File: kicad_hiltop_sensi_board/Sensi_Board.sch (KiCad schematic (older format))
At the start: 146 parts, among them J1 Conn_02x06_Counter_Clockwise, J10 Conn_ARM_JTAG_SWD_10, J2 Conn_02x06_Counter_Clockwise, J3 Conn_03x32_DIN41612, J4 Conn_02x06_Counter_Clockwise, J5 Conn_02x06_Counter_Clockwise, J6 Conn_02x06_Counter_Clockwise, J7 Conn_02x06_Counter_Clockwise, J8 Conn_02x06_Counter_Clockwise, U1 INA250A4, U2 LD1117S33TR_SOT223, U3 AT25DN512CSSHF-B, U6 LM75B

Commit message: Most major connections complete and differential tracking done on the Sensi board layout
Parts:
- added J9: Conn_02x06_Counter_Clockwise, Devtank_PCB_Lib:Molex2x06, symbol Connector:Conn_02x06_Counter_Clockwise
- added TP106, TP107, TP99: Test_Point, TestPoint:TestPoint_THTPad_D1.0mm_Drill0.5mm, symbol Sensi_Board-rescue:Test_Point-Connector
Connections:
- net labels removed: +12V_EXT
- wire segments 530 -> 537
- no-connect marks 74 -> 77
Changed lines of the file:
@@
 $EndComp
 $Comp
-L Devtank:+12V_EXT #PWR041
-U 1 1 5C4F3E8E
-P 21125 11025
-F 0 "#PWR041" H 21125 10875 50  0001 C CNN
-F 1 "+12V_EXT" H 21140 11198 50  0000 C CNN
-F 2 "" H 21125 11025 50  0001 C CNN
-F 3 "" H 21125 11025 50  0001 C CNN
-	1    21125 11025
-	1    0    0    -1
-$EndComp
-$Comp
 L Sensi_Board-rescue:Conn_03x32_DIN41612-Devtank J3
 U 1 1 5C5BC2B2
@@
 	20300 11200 21125 11200
 Wire Wire Line
-	21125 11200 21125 11100
-Wire Wire Line
 	18425 11050 17750 11050
 Wire Wire Line
@@
 	0    1    1    0
 $EndComp
-Connection ~ 21125 11200
 $Comp
 L Sensi_Board-rescue:Test_Point-Connector TP87
@@
 Wire Wire Line
 	6450 8600 6050 8600
-$Comp
-L power:PWR_FLAG #FLG0103
-U 1 1 5F48A9D2
-P 21375 11000
-F 0 "#FLG0103" H 21375 11075 50  0001 C CNN
-F 1 "PWR_FLAG" H 21375 11173 50  0000 C CNN
-F 2 "" H 21375 11000 50  0001 C CNN
-F 3 "" H 21375 11000 50  0001 C CNN
-	1    21375 11000
-	1    0    0    -1
-$EndComp
-Wire Wire Line
-	21375 11000 21375 11100
-Wire Wire Line
-	21375 11100 21125 11100
-Connection ~ 21125 11100
-Wire Wire Line
-	21125 11100 21125 11025
 Text Label 16300 9700 2    60   ~ 0
 STM_SPI1_MISO
@@
 Wire Wire Line
 	10300 7300 10650 7300
-Text Label 10650 7300 2    60   ~ 0
+Text Label 10650 7500 2    60   ~ 0
 F3+
-Text Label 10650 7200 2    60   ~ 0
+Text Label 10650 7600 2    60   ~ 0
 F3-
 Wire Wire Line
@@
 	1    0    0    -1
 $EndComp
-$Comp
-L Connector:Conn_02x06_Counter_Clockwise J5
-U 1 1 5E20E350
-P 7150 14425
-F 0 "J5" H 7200 14842 50  0000 C CNN
-F 1 "Conn_02x06_Counter_Clockwise" H 7200 14751 50  0000 C CNN
-F 2 "Devtank_PCB_Lib:Molex2x06" H 7150 14425 50  0001 C CNN
-F 3 "~" H 7150 14425 50  0001 C CNN
-F 4 "711-004" H 7150 14425 50  0001 C CNN "Devtank"
-	1    7150 14425
-	1    0    0    -1
-$EndComp
 Wire Wire Line
-	6950 14225 6525 14225
-Text Label 6525 14225 0    60   ~ 0
+	6950 14725 6525 14725
+Text Label 7875 14225 2    60   ~ 0
 ADC7
 Wire Wire Line
-	6950 14425 6525 14425
-Text Label 6525 14425 0    60   ~ 0
+	7450 14425 7875 14425
+Text Label 7875 14425 2    60   ~ 0
 ADC13
 Wire Wire Line
-	6950 14625 6525 14625
-Text Label 6525 14625 0    60   ~ 0
+	7450 14625 7875 14625
+Text Label 7875 14625 2    60   ~ 0
 ADC12
 Wire Wire Line
 	7450 14225 7875 14225
-Text Label 7875 14225 2    60   ~ 0
+Text Label 6525 14725 0    60   ~ 0
 ADC6
-NoConn ~ 7450 14525
-NoConn ~ 7450 14425
 $Comp
 L Connector:Conn_02x06_Counter_Clockwise J6
@@
 	1    0    0    -1
 $EndComp
-Text Label 10650 7500 2    60   ~ 0
+Text Label 10650 7300 2    60   ~ 0
 F2-
-Text Label 10650 7600 2    60   ~ 0
+Text Label 10650 7200 2    60   ~ 0
 F2+
 Wire Wire Line
@@
 Wire Wire Line
 	9725 7600 9725 7675
-$Comp
-L power:GND #PWR0253
-U 1 1 5E212022
-P 6825 14800
-F 0 "#PWR0253" H 6825 14550 50  0001 C CNN
-F 1 "GND" H 6830 14627 50  0000 C CNN
-F 2 "" H 6825 14800 50  0001 C CNN
-F 3 "" H 6825 14800 50  0001 C CNN
-	1    6825 14800
-	-1   0    0    -1
-$EndComp
 Wire Wire Line
 	4500 11100 4325 11100
-Wire Wire Line
-	6950 14325 6825 14325
-Wire Wire Line
-	6825 14325 6825 14525
-Wire Wire Line
-	6950 14725 6825 14725
-Connection ~ 6825 14725
-Wire Wire Line
-	6825 14725 6825 14800
-Wire Wire Line
-	6950 14525 6825 14525
-Connection ~ 6825 14525
-Wire Wire Line
-	6825 14525 6825 14725
 $Comp
 L power:+3V3 #PWR0103
@@
 L power:GND #PWR0254
 U 1 1 5DABC198
-P 7625 14325
-F 0 "#PWR0254" H 7625 14075 50  0001 C CNN
-F 1 "GND" H 7630 14152 50  0000 C CNN
-F 2 "" H 7625 14325 50  0001 C CNN
-F 3 "" H 7625 14325 50  0001 C CNN
-	1    7625 14325
+P 7625 14775
+F 0 "#PWR0254" H 7625 14525 50  0001 C CNN
+F 1 "GND" H 7630 14602 50  0000 C CNN
+F 2 "" H 7625 14775 50  0001 C CNN
+F 3 "" H 7625 14775 50  0001 C CNN
+	1    7625 14775
 	1    0    0    -1
 $EndComp
 Wire Wire Line
 	7450 14325 7625 14325
-NoConn ~ 7450 14625
-NoConn ~ 7450 14725
 Text Label 8350 8550 2    60   ~ 0
 ADC11
@@
 Text Label 10750 10250 0    60   ~ 0
 RTD2_R-
+$Comp
+L Sensi_Board-rescue:Test_Point-Connector TP99
+U 1 1 5DB957A7
+P 16300 9700
+F 0 "TP99" V 16300 9875 50  0000 L CNN
+F 1 "Test_Point" H 16358 9729 50  0001 L CNN
+F 2 "TestPoint:TestPoint_THTPad_D1.0mm_Drill0.5mm" H 16500 9700 50  0001 C CNN
+F 3 "~" H 16500 9700 50  0001 C CNN
+	1    16300 9700
+	0    1    -1   0
+$EndComp
+$Comp
+L Sensi_Board-rescue:Test_Point-Connector TP106
+U 1 1 5DC01188
+P 16300 10000
+F 0 "TP106" V 16300 10175 50  0000 L CNN
+F 1 "Test_Point" H 16358 10029 50  0001 L CNN
+F 2 "TestPoint:TestPoint_THTPad_D1.0mm_Drill0.5mm" H 16500 10000 50  0001 C CNN
+F 3 "~" H 16500 10000 50  0001 C CNN
+	1    16300 10000
+	0    1    -1   0
+$EndComp
+$Comp
+L Sensi_Board-rescue:Test_Point-Connector TP107
+U 1 1 5DC6CAD7
+P 16300 10300
+F 0 "TP107" V 16300 10475 50  0000 L CNN
+F 1 "Test_Point" H 16358 10329 50  0001 L CNN
+F 2 "TestPoint:TestPoint_THTPad_D1.0mm_Drill0.5mm" H 16500 10300 50  0001 C CNN
+F 3 "~" H 16500 10300 50  0001 C CNN
+	1    16300 10300
+	0    1    -1   0
+$EndComp
+$Comp
+L Connector:Conn_02x06_Counter_Clockwise J9
+U 1 1 5DCD8F82
+P 18075 12225
+F 0 "J9" H 18125 12642 50  0000 C CNN
+F 1 "Conn_02x06_Counter_Clockwise" H 18125 12551 50  0000 C CNN
+F 2 "Devtank_PCB_Lib:Molex2x06" H 18075 12225 50  0001 C CNN
+F 3 "~" H 18075 12225 50  0001 C CNN
+F 4 "711-004" H 18075 12225 50  0001 C CNN "Devtank"
+	1    18075 12225
+	1    0    0    -1
+$EndComp
+$Comp
+L Devtank:ADJ_DC #PWR041
+U 1 1 5DCE41C9
+P 17550 12225
+F 0 "#PWR041" H 17550 12075 50  0001 C CNN
+F 1 "ADJ_DC" H 17425 12375 50  0000 L CNN
+F 2 "" H 17550 12225 50  0000 C CNN
+F 3 "" H 17550 12225 50  0000 C CNN
+	1    17550 12225
+	0    -1   -1   0
+$EndComp
+$Comp
+L Devtank:-5V #PWR057
+U 1 1 5DD68247
+P 18700 12125
+F 0 "#PWR057" H 18700 11975 50  0001 C CNN
+F 1 "-5V" V 18715 12253 50  0000 L CNN
+F 2 "" H 18700 12125 50  0000 C CNN
+F 3 "" H 18700 12125 50  0000 C CNN
+	1    18700 12125
+	0    1    -1   0
+$EndComp
+$Comp
+L power:+5V #PWR059
+U 1 1 5DD6824D
+P 18700 12025
+F 0 "#PWR059" H 18700 11875 50  0001 C CNN
+F 1 "+5V" V 18715 12153 50  0000 L CNN
+F 2 "" H 18700 12025 50  0001 C CNN
+F 3 "" H 18700 12025 50  0001 C CNN
+	1    18700 12025
+	0    1    -1   0
+$EndComp
+Text Label 17550 12025 0    60   ~ 0
+OUT1_NO
+Text Label 17550 12125 0    60   ~ 0
+OUT1_NC
+$Comp
+L power:+3V3 #PWR053
+U 1 1 5DCE41CF
+P 17550 12425
+F 0 "#PWR053" H 17550 12275 50  0001 C CNN
+F 1 "+3V3" H 17565 12598 50  0000 C CNN
+F 2 "" H 17550 12425 50  0001 C CNN
+F 3 "" H 17550 12425 50  0001 C CNN
+	1    17550 12425
+	0    -1   -1   0
+$EndComp
+$Comp
+L power:+12V #PWR052
+U 1 1 5E067E40
+P 17550 12325
+F 0 "#PWR052" H 17550 12175 50  0001 C CNN
+F 1 "+12V" H 17565 12498 50  0000 C CNN
+F 2 "" H 17550 12325 50  0001 C CNN
+F 3 "" H 17550 12325 50  0001 C CNN
+	1    17550 12325
+	0    -1   -1   0
+$EndComp
+Wire Wire Line
+	17875 12025 17550 12025
+Wire Wire Line
+	17875 12125 17550 12125
+Wire Wire Line
+	17875 12225 17550 12225
+Wire Wire Line
+	17875 12325 17550 12325
+Wire Wire Line
+	17875 12425 17550 12425
+Wire Wire Line
+	17875 12525 17550 12525
+Wire Wire Line
+	18375 12225 18500 12225
+Wire Wire Line
+	18375 12125 18700 12125
+Wire Wire Line
+	18375 12025 18700 12025
+$Comp
+L power:GND #PWR054
+U 1 1 5EACEFF7
+P 17550 12525
+F 0 "#PWR054" H 17550 12275 50  0001 C CNN
+F 1 "GND" H 17555 12352 50  0000 C CNN
+F 2 "" H 17550 12525 50  0001 C CNN
+F 3 "" H 17550 12525 50  0001 C CNN
+	1    17550 12525
+	1    0    0    -1
+$EndComp
+$Comp
+L power:GND #PWR056
+U 1 1 5EACF7D8
+P 18500 12500
+F 0 "#PWR056" H 18500 12250 50  0001 C CNN
+F 1 "GND" H 18505 12327 50  0000 C CNN
+F 2 "" H 18500 12500 50  0001 C CNN
+F 3 "" H 18500 12500 50  0001 C CNN
+	1    18500 12500
+	1    0    0    -1
+$EndComp
+Wire Wire Line
+	18500 12500 18500 12225
+$Comp
+L power:GND #PWR0150
+U 1 1 5DC4CA85
+P 6925 14875
+F 0 "#PWR0150" H 6925 14625 50  0001 C CNN
+F 1 "GND" H 6930 14702 50  0000 C CNN
+F 2 "" H 6925 14875 50  0001 C CNN
+F 3 "" H 6925 14875 50  0001 C CNN
+	1    6925 14875
+	1    0    0    -1
+$EndComp
+Wire Wire Line
+	7625 14325 7625 14525
+Wire Wire Line
+	7450 14525 7625 14525
+Connection ~ 7625 14525
+Wire Wire Line
+	7625 14525 7625 14725
+Wire Wire Line
+	7450 14725 7625 14725
+Connection ~ 7625 14725
+Wire Wire Line
+	7625 14725 7625 14775
+$Comp
+L Connector:Conn_02x06_Counter_Clockwise J5
+U 1 1 5E20E350
+P 7150 14425
+F 0 "J5" H 7200 14842 50  0000 C CNN
+F 1 "Conn_02x06_Counter_Clockwise" H 7200 14751 50  0000 C CNN
+F 2 "Devtank_PCB_Lib:Molex2x06" H 7150 14425 50  0001 C CNN
+F 3 "~" H 7150 14425 50  0001 C CNN
+F 4 "711-004" H 7150 14425 50  0001 C CNN "Devtank"
+	1    7150 14425
+	1    0    0    -1
+$EndComp
+NoConn ~ 6950 14225
+NoConn ~ 6950 14325
+NoConn ~ 6950 14425
+NoConn ~ 6950 14525
+Wire Wire Line
+	6925 14875 6925 14625
+Wire Wire Line
+	6925 14625 6950 14625
+NoConn ~ 18375 12325
+NoConn ~ 18375 12425
+NoConn ~ 18375 12525
 $EndSCHEMATC

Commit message: Most routing on Sensi Board complete
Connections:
- net +12V: now also J9.9 (Pin_9); no longer J9.4 (Pin_4)
- net +3V3: now also J9.10 (Pin_10); no longer J9.5 (Pin_5)
- net +5V: now also J9.7 (Pin_7); no longer J9.12 (Pin_12)
- net ADJ_DC: now also J9.2 (Pin_2); no longer J9.3 (Pin_3)
- net GND: now also J1.10 (Pin_10), J1.11 (Pin_11), J2.8 (Pin_8), J9.5 (Pin_5), J9.8 (Pin_8); no longer J1.8 (Pin_8), J1.9 (Pin_9), J2.11 (Pin_11), J9.10 (Pin_10), J9.6 (Pin_6)
- net GPIO10: now also J2.10 (Pin_10); no longer J2.9 (Pin_9)
- net GPIO11: now also J2.11 (Pin_11); no longer J2.8 (Pin_8)
- net GPIO12: now also J2.12 (Pin_12); no longer J2.7 (Pin_7)
- net GPIO3: now also J1.8 (Pin_8); no longer J1.11 (Pin_11)
- net GPIO4: now also J1.7 (Pin_7); no longer J1.12 (Pin_12)
- net GPIO9: now also J2.9 (Pin_9); no longer J2.10 (Pin_10)
- net HS_OUT1: now also J1.9 (Pin_9); no longer J1.10 (Pin_10)
- net HS_OUT2: now also J1.12 (Pin_12); no longer J1.7 (Pin_7)
- net HS_OUT3: now also J2.7 (Pin_7); no longer J2.12 (Pin_12)
- net OUT1_NC: now also J9.1 (Pin_1); no longer J9.2 (Pin_2)
- net OUT1_NO: now also J9.12 (Pin_12); no longer J9.1 (Pin_1)
- net RTD1_F-: now also J8.11 (Pin_11); no longer J8.8 (Pin_8)
- net RTD1_R-: now also J8.12 (Pin_12); no longer J8.7 (Pin_7)
- net RTD2_F+: now also J8.7 (Pin_7); no longer J8.12 (Pin_12)
- net RTD2_R+: now also J8.8 (Pin_8); no longer J8.11 (Pin_11)
- net RTD3_F-: now also J7.11 (Pin_11); no longer J7.8 (Pin_8)
- net RTD3_R-: now also J7.12 (Pin_12); no longer J7.7 (Pin_7)
- net RTD4_F+: now also J7.7 (Pin_7); no longer J7.12 (Pin_12)
- net RTD4_R+: now also J7.8 (Pin_8); no longer J7.11 (Pin_11)
- net TH2+: now also J4.12 (Pin_12); no longer J4.7 (Pin_7)
- net TH2-: now also J4.11 (Pin_11); no longer J4.8 (Pin_8)
- net TH4+: now also J4.8 (Pin_8); no longer J4.11 (Pin_11)
- net TH4-: now also J4.7 (Pin_7); no longer J4.12 (Pin_12)
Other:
- moved on the sheet: R37, R38

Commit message: Sensi board with references visible and without stitching vias
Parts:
- C12, C9: Devtank 105-002 -> 105-019
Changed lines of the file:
@@
 F 2 "Capacitor_SMD:C_0402_1005Metric" H 18613 9900 50  0001 C CNN
 F 3 "" H 18575 10050 50  0001 C CNN
-F 4 "105-002" H -350 1050 50  0001 C CNN "Devtank"
+F 4 "105-019" H -350 1050 50  0001 C CNN "Devtank"
 	1    18575 10050
 	0    1    1    0
@@
 F 2 "Capacitor_SMD:C_0402_1005Metric" H 21913 2975 50  0001 C CNN
 F 3 "" H 21875 3125 50  0001 C CNN
-F 4 "105-002" H 0   0   50  0001 C CNN "Devtank"
+F 4 "105-019" H 0   0   50  0001 C CNN "Devtank"
 	1    21875 3125
 	0    1    1    0

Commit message: Changes to Sensi board after review
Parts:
- removed J10: Conn_ARM_JTAG_SWD_10, Connector_PinHeader_2.54mm:PinHeader_2x05_P2.54mm_Vertical, symbol Connector:Conn_ARM_JTAG_SWD_10
- removed J6: Conn_02x06_Counter_Clockwise, Devtank_PCB_Lib:Molex2x06, symbol Connector:Conn_02x06_Counter_Clockwise
- added C? (x5): 100nF, symbol device:C
- added J10: Conn_02x05_Counter_Clockwise, Connector_PinHeader_2.54mm:PinHeader_2x05_P2.54mm_Vertical, symbol Connector:Conn_02x05_Counter_Clockwise
- added J?: Conn_02x10_Counter_Clockwise, symbol Connector:Conn_02x10_Counter_Clockwise
- added JP? (x4): Jumper_NC_Small, symbol device:Jumper_NC_Small
- added R? (x4): 0R, symbol device:R
- C24: Devtank 105-019 -> (none)
- R39, R40: Devtank 101-015 -> (none)
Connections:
- net GPIO11 is gone; now on net GPIO1: J2.11 (Pin_11), TP47.1
- net GPIO12 is gone; now on net GPIO2: J2.12 (Pin_12), TP48.1
- net +12V: now also C?.1, R?.1, R?.1
- net +3V3: now also R40.1, C?.1, J10.1 (Pin_1); no longer R40.2
- net +5V: now also C?.1
- net -5V: now also C?.1
- net ADJ_DC: now also C?.1, R?.1, R?.1
- net F1+: now also J?.3 (Pin_3)
- net F1-: now also J?.4 (Pin_4), JP?.1
- net F2+: now also J?.8 (Pin_8)
- net F2-: now also J?.9 (Pin_9), JP?.1
- net F3+: now also J?.18 (Pin_18)
- net F3-: now also J?.17 (Pin_17), JP?.1
- net F4+: now also J?.13 (Pin_13)
- net F4-: now also J?.12 (Pin_12), JP?.1
- net GND: now also J9.3 (Pin_3), J9.4 (Pin_4), J9.6 (Pin_6), R39.1, C?.2, C?.2, C?.2, C?.2, C?.2, J10.3 (Pin_3), J10.5 (Pin_5), J10.9 (Pin_9), J?.1 (Pin_1), J?.10 (Pin_10), J?.11 (Pin_11), J?.15 (Pin_15), J?.16 (Pin_16), J?.20 (Pin_20), J?.5 (Pin_5), J?.6 (Pin_6), JP?.2, JP?.2, JP?.2, JP?.2; no longer R39.2
- net GPIO1: no longer J1.5 (Pin_5), TP37.1, TP91.1
- net GPIO2: no longer J1.6 (Pin_6), TP38.1, TP92.1
- net STM_RESET: now also J10.10 (Pin_10)
- net SWD_IO: now also R40.2, J10.2 (Pin_2); no longer R40.1
- net SWD_SCK: now also R39.2, J10.4 (Pin_4); no longer R39.1
- net 5V_ADC10 renamed AIN_CH2
- net AIN_CH2: now also J5.10 (Pin_10)
- net 5V_ADC11 renamed AIN_CH3
- net AIN_CH3: now also J5.8 (Pin_8)
- net 5V_ADC12 renamed AIN_CH4
- net AIN_CH4: now also J5.6 (Pin_6)
- net 5V_ADC9 renamed AIN_CH1
- net AIN_CH1: now also J5.12 (Pin_12)
- net ADC1 renamed TH3_OUT
- net ADC10 renamed TH2_OUT
- net ADC11 renamed TH1_OUT
- net ADC12 renamed AIN_BUF_CH3
- net AIN_BUF_CH3: no longer J5.8 (Pin_8)
- net ADC13 renamed AIN_BUF_CH2
- net AIN_BUF_CH2: no longer J5.10 (Pin_10)
- net ADC2 renamed F4_OUT
- net ADC3 renamed F3_OUT
- net ADC4 renamed F2_OUT
- net ADC5 renamed F1_OUT
- net ADC6 renamed AIN_BUF_CH4
- net AIN_BUF_CH4: no longer J5.6 (Pin_6)
- net ADC7 renamed AIN_BUF_CH1
- net AIN_BUF_CH1: no longer J5.12 (Pin_12)
- net ADC9 renamed TH4_OUT
- net GPIO10 renamed SB2
- net GPIO3 renamed RTD2_INT
- net GPIO4 renamed RTD2_CS
- net GPIO5 renamed RTD3_INT
- net GPIO6 renamed RTD3_CS
- net GPIO7 renamed RTD4_INT
- net GPIO8 renamed RTD4_CS
- net GPIO9 renamed SB1
- new net: J?.14 (Pin_14), J?.19 (Pin_19), R?.2, R?.2
- new net: J?.2 (Pin_2), J?.7 (Pin_7), R?.2, R?.2
- new net RTD1_CS: J1.6 (Pin_6), TP38.1, TP92.1
- new net RTD1_INT: J1.5 (Pin_5), TP37.1, TP91.1
- no-connect marks 77 -> 73
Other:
- note added: "Default Config 3 Wire\n"
- note added: "J1\nLeft Position\nRight Position\nLeft Position"
- note added: "J2\nClose\nClose\nOpen"
- note added: "J3\nClose\nOpen\nOpen"
- note added: "JTAG Header\n"
- note added: "RTD Config\n2 Wire\n3 Wire\n4 Wire"
- moved on the sheet: J9, TP55, TP56, TP57, TP58, TP91, TP92, TP93, TP94, TP95, TP96, TP97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

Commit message: Sensi board schematic updated from comments
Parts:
- removed TP19, TP20, TP21, TP22, TP23, TP24, TP41, TP42, TP43, TP44, TP47, TP48: Test_Point, TestPoint:TestPoint_THTPad_D1.0mm_Drill0.5mm, symbol Sensi_Board-rescue:Test_Point-Connector
- gave numbers to parts that had none: 14
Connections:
- net F2+ is gone; now on net F1+: J6.8 (Pin_8), TP50.1
- net F4+ is gone; now on net F3+: J6.13 (Pin_13), TP54.1
- net F1+: now also J6.2 (Pin_2), J6.7 (Pin_7), R41.2, R44.2
- net F3+: now also J6.14 (Pin_14), J6.19 (Pin_19), R45.2, R46.2
- net GPIO1: now also TP37.1; no longer J2.11 (Pin_11)
- net GPIO1_EXT: now also J1.1 (Pin_1)
- net GPIO2: now also TP38.1; no longer J2.12 (Pin_12)
- net GPIO2_EXT: now also J1.2 (Pin_2)
- net GPIO3_EXT: now also J1.3 (Pin_3)
- net GPIO4_EXT: now also J1.4 (Pin_4)
- net GPIO5_EXT: now also J2.9 (Pin_9), R37.2
- net GPIO6_EXT: now also J2.10 (Pin_10), R38.2
- net RTD1_CS: no longer J1.6 (Pin_6), TP38.1
- net RTD1_INT: no longer J1.5 (Pin_5), TP37.1
- net RTD2_CS: no longer J1.7 (Pin_7), TP40.1
- net RTD2_INT: no longer J1.8 (Pin_8), TP39.1
- net RTD3_CS: no longer J1.2 (Pin_2)
- net RTD3_INT: no longer J1.1 (Pin_1)
- net RTD4_CS: no longer J1.4 (Pin_4)
- net RTD4_INT: no longer J1.3 (Pin_3)
- net SB1: no longer J2.9 (Pin_9), R37.2
- net SB2: no longer J2.10 (Pin_10), R38.2
- new net GPIO3: TP39.1
- new net GPIO4: TP40.1
- no-connect marks 73 -> 80
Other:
- note removed: "Default Config 3 Wire\n"
- note removed: "J1\nLeft Position\nRight Position\nLeft Position"
- note removed: "J2\nClose\nClose\nOpen"
- note removed: "J3\nClose\nOpen\nOpen"
- note removed: "RTD Config\n2 Wire\n3 Wire\n4 Wire"
- moved on the sheet: J5, R38, R39, TP45, TP46

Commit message: Updated sensi board layout
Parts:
- removed J1, J2, J4, J5, J7, J8, J9: Conn_02x06_Counter_Clockwise, Devtank_PCB_Lib:Molex2x06, symbol Connector:Conn_02x06_Counter_Clockwise
- removed TP50: Test_Point, TestPoint:TestPoint_THTPad_D1.0mm_Drill0.5mm, symbol Sensi_Board-rescue:Test_Point-Connector
- added J1, J2, J4, J5, J7, J8, J9: Conn_02x06_Top_Bottom, Devtank_PCB_Lib:Molex2x06, symbol Connector:Conn_02x06_Top_Bottom
- added TP19: Test_Point, TestPoint:TestPoint_THTPad_D1.0mm_Drill0.5mm, symbol Sensi_Board-rescue:Test_Point-Connector
- C26, C27, C28, C29, C30: footprint (none) -> Capacitor_SMD:C_0402_1005Metric
- J6: footprint (none) -> Devtank_PCB_Lib:Molex_Milligrid_2x10
- JP2, JP3, JP4, JP5: footprint (none) -> Connector_PinHeader_1.27mm:PinHeader_1x02_P1.27mm_Vertical
- R41, R44, R45, R46: footprint (none) -> Resistor_SMD:R_0805_2012Metric
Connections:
- net +12V: now also J9.10 (Pin_10)
- net +3V3: now also J9.9 (Pin_9)
- net +5V: now also J5.1 (Pin_1), J5.2 (Pin_2), J5.3 (Pin_3), J5.4 (Pin_4), J9.12 (Pin_12)
- net -5V: now also J9.8 (Pin_8)
- net ADJ_DC: now also J9.2 (Pin_2)
- net AIN_CH1: now also J5.10 (Pin_10)
- net AIN_CH2: now also J5.7 (Pin_7)
- net AIN_CH3: now also J5.11 (Pin_11)
- net AIN_CH4: now also J5.12 (Pin_12)
- net F1+: now also TP19.1
- net F3-: now also J6.12 (Pin_12), JP5.1; no longer J6.17 (Pin_17), JP4.1
- net F4-: now also J6.17 (Pin_17), JP4.1; no longer J6.12 (Pin_12), JP5.1
- net GND: now also J1.11 (Pin_11), J1.5 (Pin_5), J2.1 (Pin_1), J2.10 (Pin_10), J2.3 (Pin_3), J2.5 (Pin_5), J2.7 (Pin_7), J4.3 (Pin_3), J4.4 (Pin_4), J4.5 (Pin_5), J4.6 (Pin_6), J5.5 (Pin_5), J5.6 (Pin_6), J5.8 (Pin_8), J5.9 (Pin_9), J7.10 (Pin_10), J7.4 (Pin_4), J8.10 (Pin_10), J8.4 (Pin_4), J9.11 (Pin_11), J9.3 (Pin_3), J9.4 (Pin_4), J9.5 (Pin_5), J9.6 (Pin_6)
- net GPIO1_EXT: now also J1.4 (Pin_4)
- net GPIO2_EXT: now also J1.3 (Pin_3)
- net GPIO3_EXT: now also J1.2 (Pin_2)
- net GPIO4_EXT: now also J1.1 (Pin_1)
- net GPIO5_EXT: now also R38.2, J2.8 (Pin_8); no longer R37.2
- net GPIO6_EXT: now also R37.2, J2.9 (Pin_9); no longer R38.2
- net HS_OUT1: now also J1.6 (Pin_6)
- net HS_OUT2: now also J1.12 (Pin_12)
- net HS_OUT3: now also J2.4 (Pin_4)
- net HS_OUT4: now also J2.2 (Pin_2)
- net OUT1_NC: now also J2.6 (Pin_6), J9.1 (Pin_1)
- net OUT1_NO: now also J2.12 (Pin_12), J9.7 (Pin_7)
- net RTD1_F+: now also J8.1 (Pin_1)
- net RTD1_F-: now also J8.8 (Pin_8)
- net RTD1_R+: now also J8.2 (Pin_2)
- net RTD1_R-: now also J8.7 (Pin_7)
- net RTD2_F+: now also J8.12 (Pin_12)
- net RTD2_F-: now also J8.5 (Pin_5)
- net RTD2_R+: now also J8.11 (Pin_11)
- net RTD2_R-: now also J8.6 (Pin_6)
- net RTD3_F+: now also J7.1 (Pin_1)
- net RTD3_F-: now also J7.8 (Pin_8)
- net RTD3_R+: now also J7.2 (Pin_2)
- net RTD3_R-: now also J7.7 (Pin_7)
- net RTD4_F+: now also J7.12 (Pin_12)
- net RTD4_F-: now also J7.5 (Pin_5)
- net RTD4_R+: now also J7.11 (Pin_11)
- net RTD4_R-: now also J7.6 (Pin_6)
- net TH1+: now also J4.2 (Pin_2)
- net TH1-: now also J4.1 (Pin_1)
- net TH2+: now also J4.11 (Pin_11)
- net TH2-: now also J4.12 (Pin_12)
- net TH3+: now also J4.7 (Pin_7)
- net TH3-: now also J4.8 (Pin_8)
- net TH4+: now also J4.9 (Pin_9)
- net TH4-: now also J4.10 (Pin_10)
- no-connect marks 80 -> 72

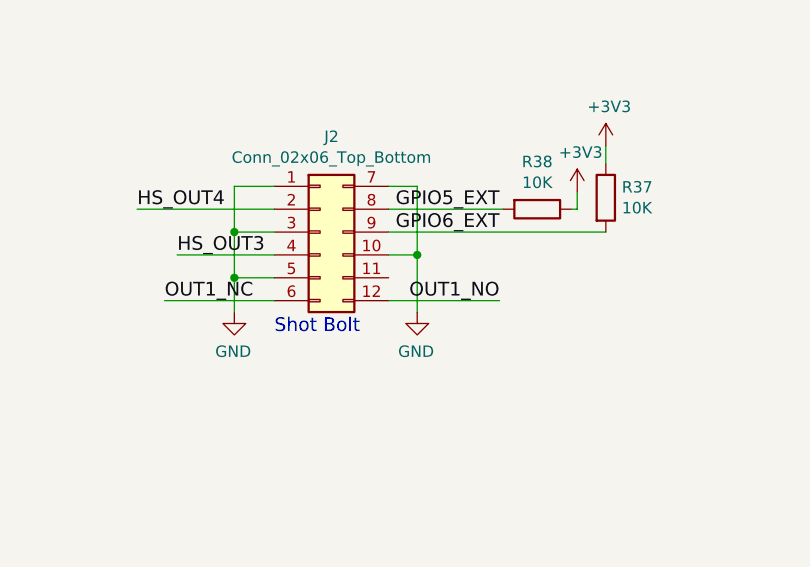
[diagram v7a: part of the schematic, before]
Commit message: Missing connection added to Sensi Board
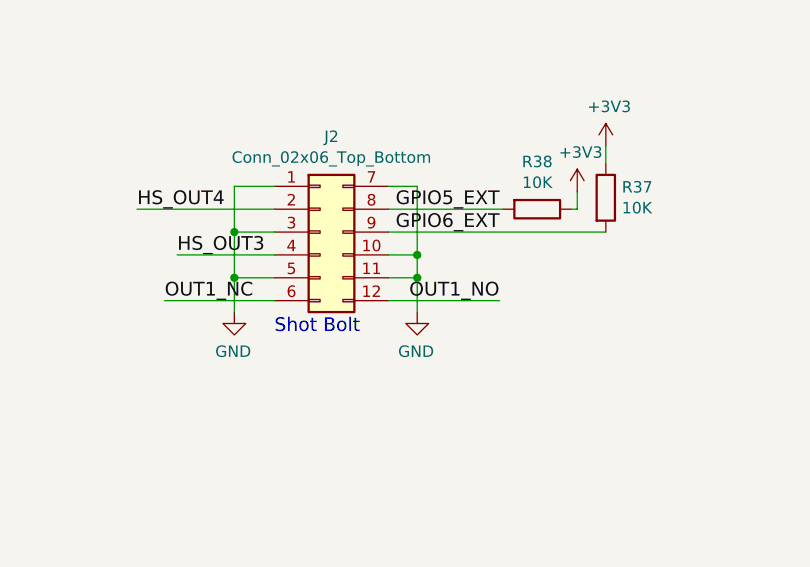
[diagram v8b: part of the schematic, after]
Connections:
- net GND: now also J2.11 (Pin_11)
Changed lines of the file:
@@
 	5000 11400 5125 11400
 Wire Wire Line
-	5125 11400 5125 11650
+	5125 11400 5125 11500
 Text Label 2650 11625 2    60   ~ 0
 HS_OUT2
@@
 	4325 11100 4500 11100
 Connection ~ 4325 11300
+Wire Wire Line
+	5000 11500 5125 11500
+Connection ~ 5125 11500
+Wire Wire Line
+	5125 11500 5125 11650
 $EndSCHEMATC
